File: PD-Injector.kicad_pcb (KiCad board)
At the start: 2 copper layers, 22.6 x 28.5 mm, 16 parts

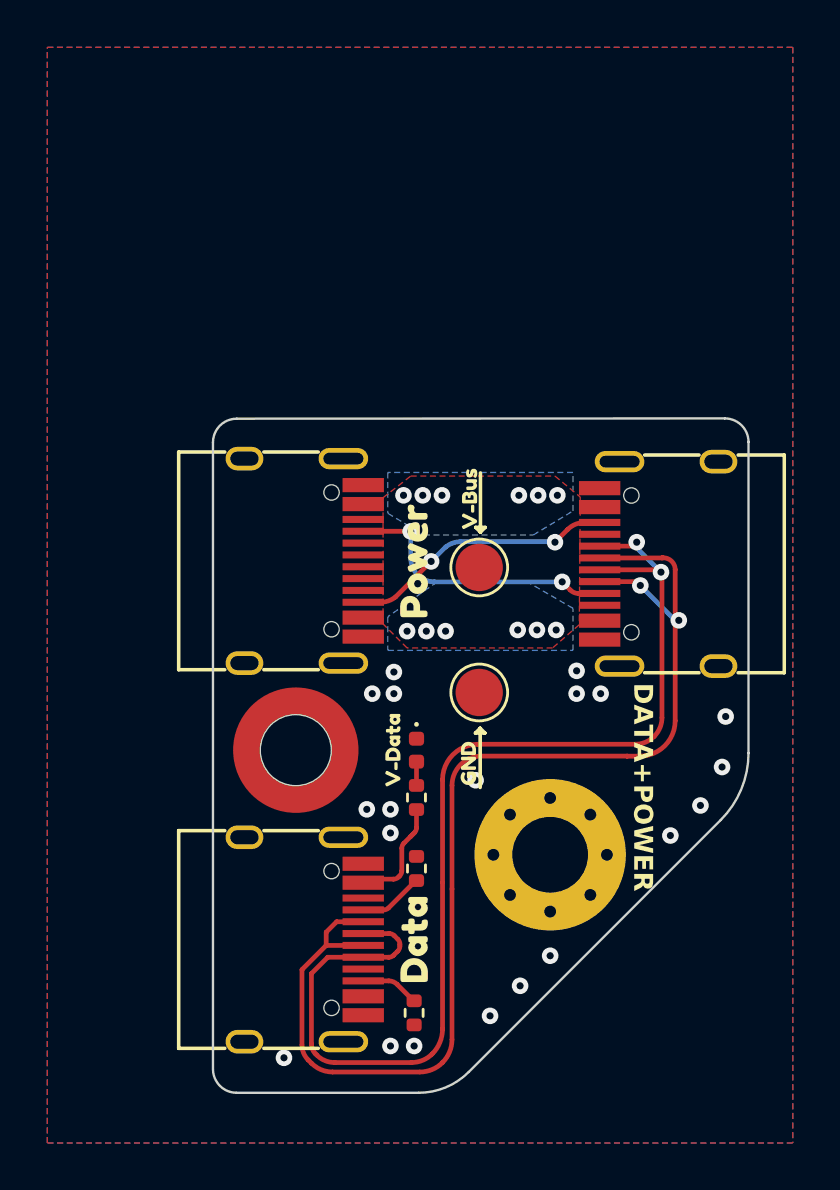
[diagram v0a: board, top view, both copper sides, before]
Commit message: switch USB-C part
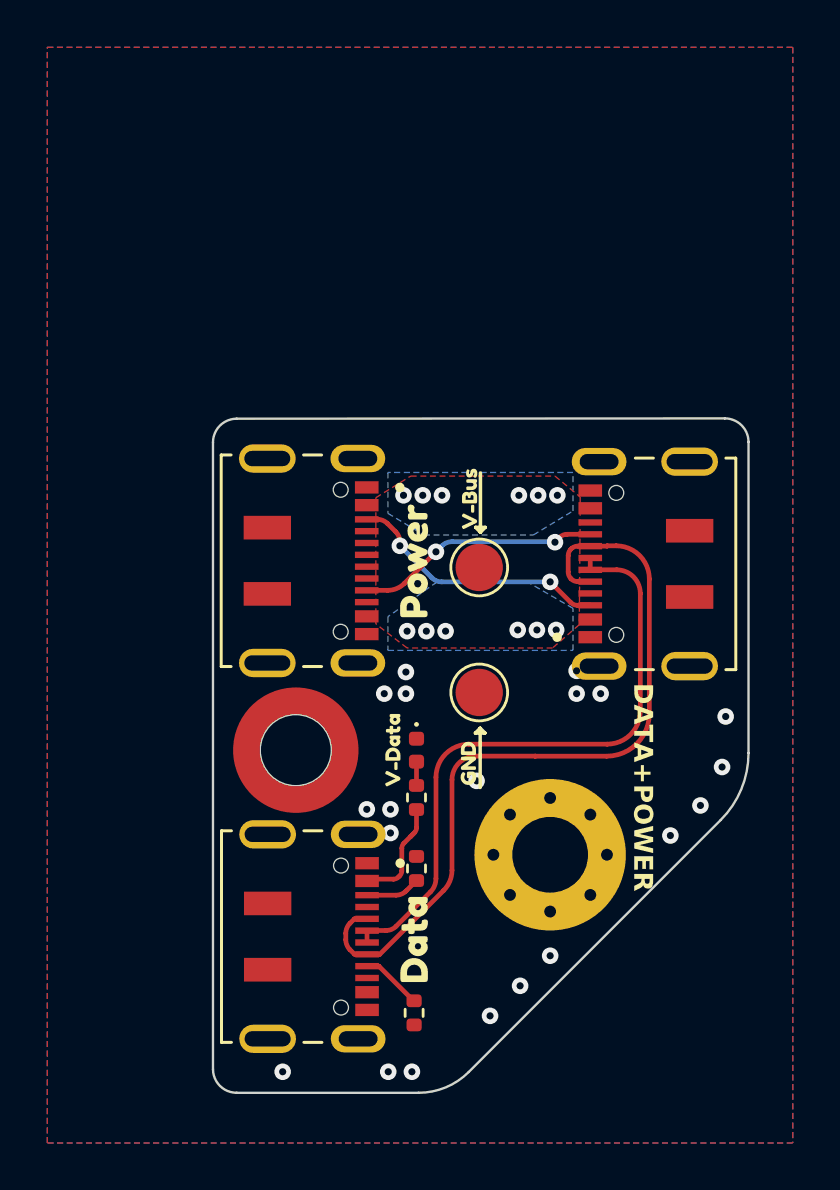
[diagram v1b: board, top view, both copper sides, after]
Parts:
- USB-C1, USB-C2, USB-C3: footprint PD-Injector_SMD:USB_C_Receptacle_GT-USB-7010 -> PD-Injector:JAE_DX07S016JA1R1500
- moved USB-C3 2.45 mm to (173.5, 78.1)
- moved USB-C2 2.21 mm to (161.9, 93.9)
- moved USB-C1 2.20 mm to (161.9, 78.0)
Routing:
- net /D+: track 49.3 -> 26.6 mm, vias 2 -> 0
- net /D-: track 51.7 -> 33.7 mm, vias 2 -> 0
- net /CC1P: track 11.8 -> 11.1 mm
- net /CC2P: track 11.3 -> 10.8 mm

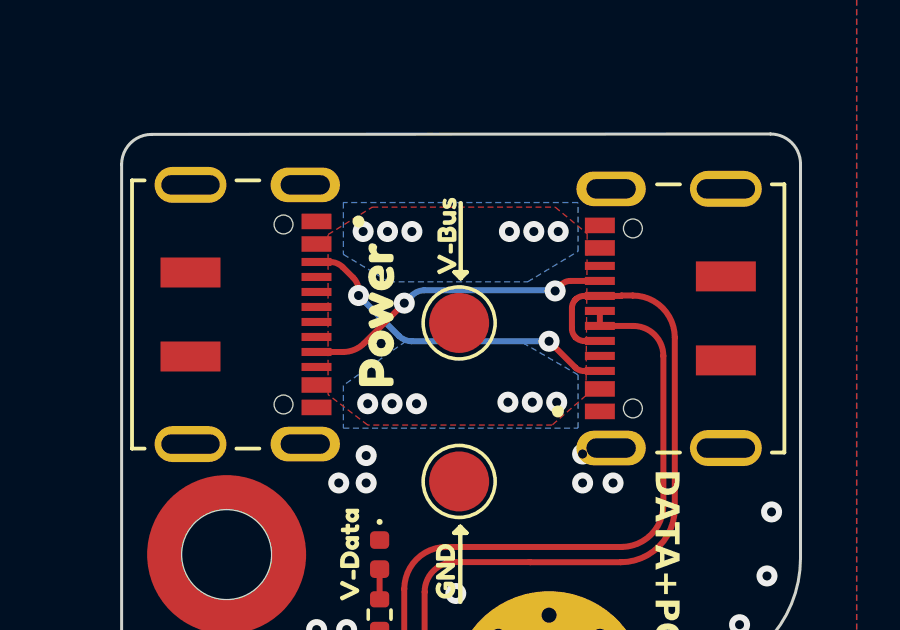
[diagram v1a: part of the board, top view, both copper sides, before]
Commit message: more vbus copper
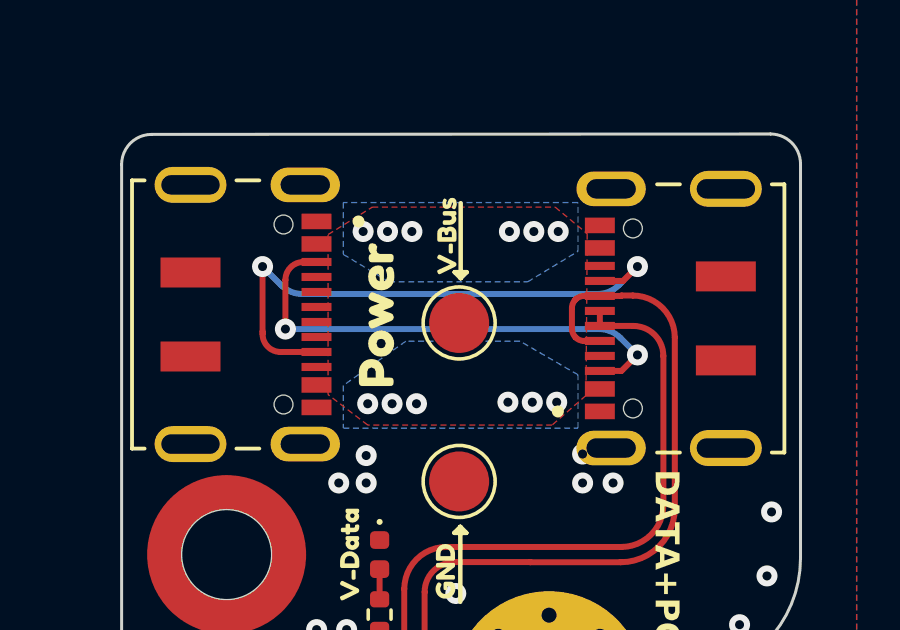
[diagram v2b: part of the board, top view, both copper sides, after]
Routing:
- net /CC2P: track 10.8 -> 19.0 mm
- net /CC1P: track 11.1 -> 16.5 mm

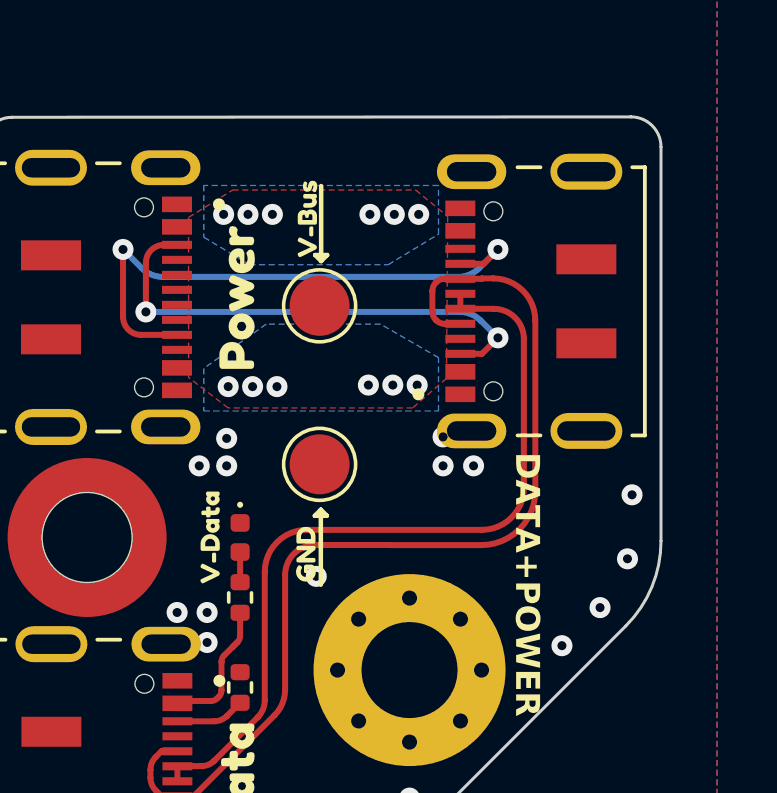
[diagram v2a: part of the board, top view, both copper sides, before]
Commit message: add USB2.0 test pads
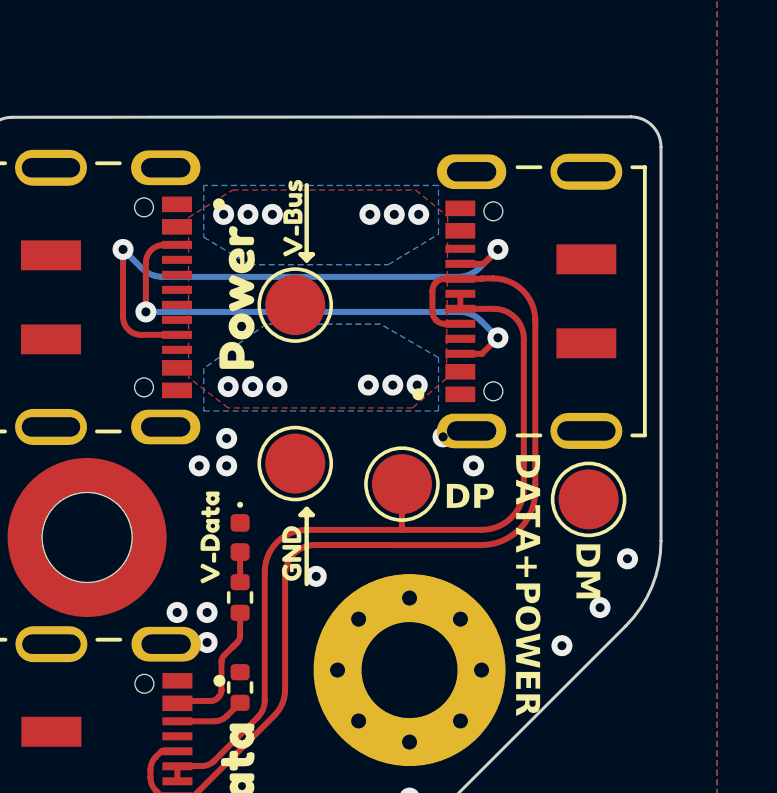
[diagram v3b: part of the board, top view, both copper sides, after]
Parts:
- added TP2: TestPoint, TestPoint:TestPoint_Pad_D2.0mm, F.Cu at (176.7, 84.7)
- added TP2: TestPoint, TestPoint:TestPoint_Pad_D2.0mm, F.Cu at (170.5, 84.2)
- moved TP1 0.81 mm to (166.9, 78.3)
- moved TP2 0.81 mm to (166.9, 83.5)
- moved kibuzzard-6334B838 0.48 mm to (166.9, 75.4)
- moved kibuzzard-6334B904 0.47 mm to (166.8, 86.5)
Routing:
- net /D+: track 26.6 -> 27.8 mm
- net /D-: track 33.7 -> 34.4 mm
- net GND: vias 20 -> 18
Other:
- board text added: "DM"
- board text added: "DP"
